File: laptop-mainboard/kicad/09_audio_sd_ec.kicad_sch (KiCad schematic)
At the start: 17 parts, among them U39 ALC256_Codec, U40 GL3224_SD, U41 IT5570E_EC, U42 W25Q128_ECFW

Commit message: Rev B: echte AM5-Pinbelegung, Kleinteile, EliteBook-850-G7-Format
- AM5-Pinmap (1718 Pins, WikiChip/Wikimedia Public Domain) als CSV,
  Sockel-Footprint mit echten Padnamen und 1708 Signal-Netzen im Board
- Blatt 10: MLCC-Baenke, 11 ESD-Arrays, USB2-Chokes, Straps; 48-MHz-Quarz;
  beidseitige Bestueckung (B.Cu) mit Kollisionspruefung pro Seite
- Board 340x112mm im EliteBook-850-G7-Layout: USB-C-100W-PD an der
  Barrel-Jack-Position, TB4/HDMI/USB-A/RJ45 rechts, USB-A/Klinke links,
  HP-Akku 3S/56Wh, HP-FPC-Steckplaetze (Pinouts zu verifizieren)
- GND-Stitching-Vias, MDI-/DP-Korridore, 645 Board-Netze
- Renderer tools/render_board.py erzeugt docs/board_render.png
- Doku: elitebook.md neu, grenzen.md/README/power/layout aktualisiert

Co-Authored-By: Claude Fable 5 <noreply@anthropic.com>
Claude-Session: https://claude.ai/code/session_01E8mU1RUAv938Hs69waADCc
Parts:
- removed J_SD: SD_Slot_PushPush, laptop_mainboard:SD_PUSH, symbol lm:SD_Slot_PushPush_J_SD
- removed U40: GL3224_SD, laptop_mainboard:QFN48_6x6, symbol lm:GL3224_SD_U40
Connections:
- net EN_USBC2 is gone; now on net TB_PWR_EN: U41.40 (TB_PWR_EN)
- net EN_USBC3 is gone; now on net TB_FORCE_PWR: U41.41 (TB_FORCE_PWR)
- net LAN2_PERST# is gone; now on net NVME2_DEVSLP: U41.49 (SSD2_DEVSLP)
- net +3V3_ALW: now also U41.66 (VCC3V3_ALW); no longer U41.69 (VCC3V3_ALW)
- net ECF_CLK: now also U41.63 (ECSPI_CLK); no longer U41.66 (ECSPI_CLK)
- net ECF_CS#: now also U41.62 (ECSPI_CS#); no longer U41.65 (ECSPI_CS#)
- net ECF_MISO: now also U41.65 (ECSPI_MISO); no longer U41.68 (ECSPI_MISO)
- net ECF_MOSI: now also U41.64 (ECSPI_MOSI); no longer U41.67 (ECSPI_MOSI)
- net EDP_BL_EN: now also U41.59 (BL_EN); no longer U41.62 (BL_EN)
- net EDP_BL_PWM: now also U41.60 (BL_PWM); no longer U41.63 (BL_PWM)
- net FAN1_PWM: now also U41.55 (FAN1_PWM); no longer U41.58 (FAN1_PWM)
- net FAN1_TACH: now also U41.56 (FAN1_TACH); no longer U41.59 (FAN1_TACH)
- net FAN2_PWM: now also U41.57 (FAN2_PWM); no longer U41.60 (FAN2_PWM)
- net FAN2_TACH: now also U41.58 (FAN2_TACH); no longer U41.61 (FAN2_TACH)
- net GND: now also U41.67 (GND); no longer U41.70 (GND)
- net KB_BL_CTL: now also U41.61 (KB_BL_CTL); no longer U41.64 (KB_BL_CTL)
- net LAN1_PERST#: now also U41.46 (PE_RST_LAN1#); no longer U41.48 (PE_RST_LAN1#)
- net NVME1_DEVSLP: now also U41.48 (SSD1_DEVSLP); no longer U41.51 (SSD1_DEVSLP)
- net NVME1_PERST#: now also U41.43 (PE_RST_SSD1#); no longer U41.45 (PE_RST_SSD1#)
- net NVME2_DEVSLP: no longer U41.52 (SSD2_DEVSLP)
- net NVME2_PERST#: now also U41.44 (PE_RST_SSD2#); no longer U41.46 (PE_RST_SSD2#)
- net PG_3V3: now also U41.54 (PG_3V3); no longer U41.57 (PG_3V3)
- net PG_5V: now also U41.53 (PG_5V); no longer U41.56 (PG_5V)
- net TB_FORCE_PWR: no longer U41.43 (TB_FORCE_PWR)
- net TB_PERST#: now also U41.45 (PE_RST_TB#); no longer U41.47 (PE_RST_TB#)
- net TB_PWR_EN: no longer U41.42 (TB_PWR_EN)
- net TB_RESET#: now also U41.42 (TB_RESET#); no longer U41.44 (TB_RESET#)
- net VRM_PWRGD: now also U41.52 (VRM_PWRGD); no longer U41.55 (VRM_PWRGD)
- net WIFI_PERST#: now also U41.47 (PE_RST_WIFI#); no longer U41.50 (PE_RST_WIFI#)
- net W_DISABLE1#: now also U41.50 (W_DISABLE1#); no longer U41.53 (W_DISABLE1#)
- net W_DISABLE2#: now also U41.51 (W_DISABLE2#); no longer U41.54 (W_DISABLE2#)
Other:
- note added: "Audio: ALC256 am SoC-HDA-Link; Klinke links wie beim 850 G7."
- note added: "HP-FPC-Pinouts (Tastatur/Touchpad/Akku): docs/elitebook.md."
- note removed: "Audio: ALC256 am SoC-HDA-Link; Klinke = AUX-Kombiport."
- note removed: "SD-Leser GL3224 an USB3-Port 5 des SoC (UHS-II faehig)."
- title: Audio / SD-Leser / Embedded Controller -> Audio / Embedded Controller

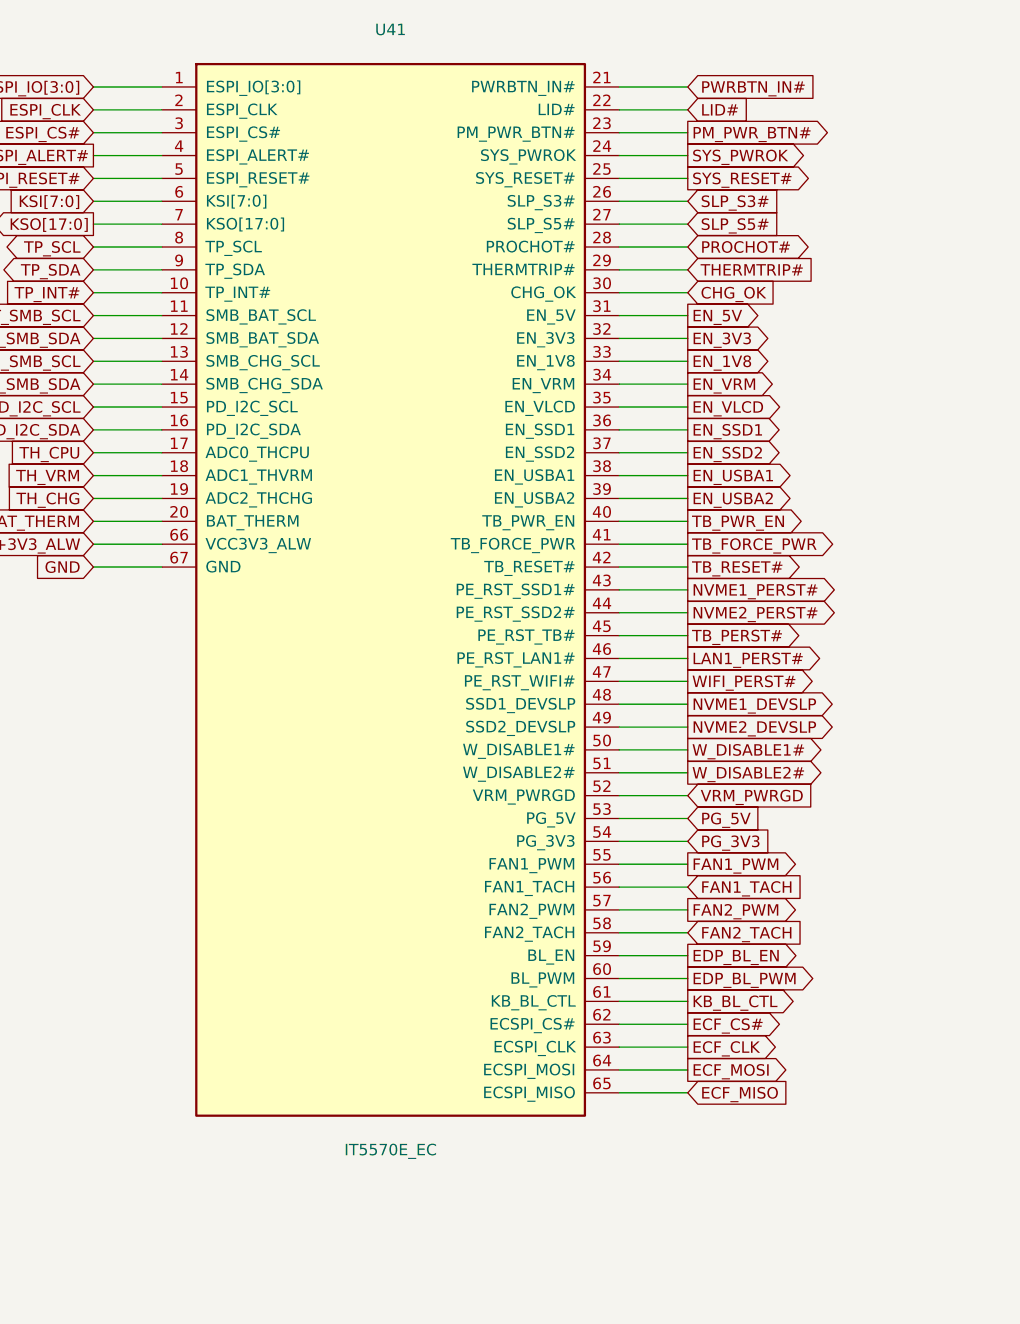
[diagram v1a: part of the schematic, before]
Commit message: Portlayout nach Fotos des Originalgeraets korrigiert
- Rechte Kante hinten->vorn: USB-C-Ladeport 100W (Barrel-Position,
  eigener TPS65987D + Config-Flash, neues Blatt 07_ladeport), USB-A,
  HDMI, 2x USB-C Thunderbolt 4 nebeneinander (JHL8540)
- Kein RJ45 (Original hat keines): Ethernet entfernt, G0/G1 Reserve
- TPS65988 nur noch Source fuer die TB-Ports; breite VBUS_IN-Trasse
  vom Ladeport zum BQ25731
- Interne Anschlusspositionen des Original-Mainboards (Nutzerfoto)
  als Referenztabelle in docs/elitebook.md dokumentiert
- Doku, Blockdiagramm, BOM und Rendering aktualisiert

Co-Authored-By: Claude Fable 5 <noreply@anthropic.com>
Claude-Session: https://claude.ai/code/session_01E8mU1RUAv938Hs69waADCc
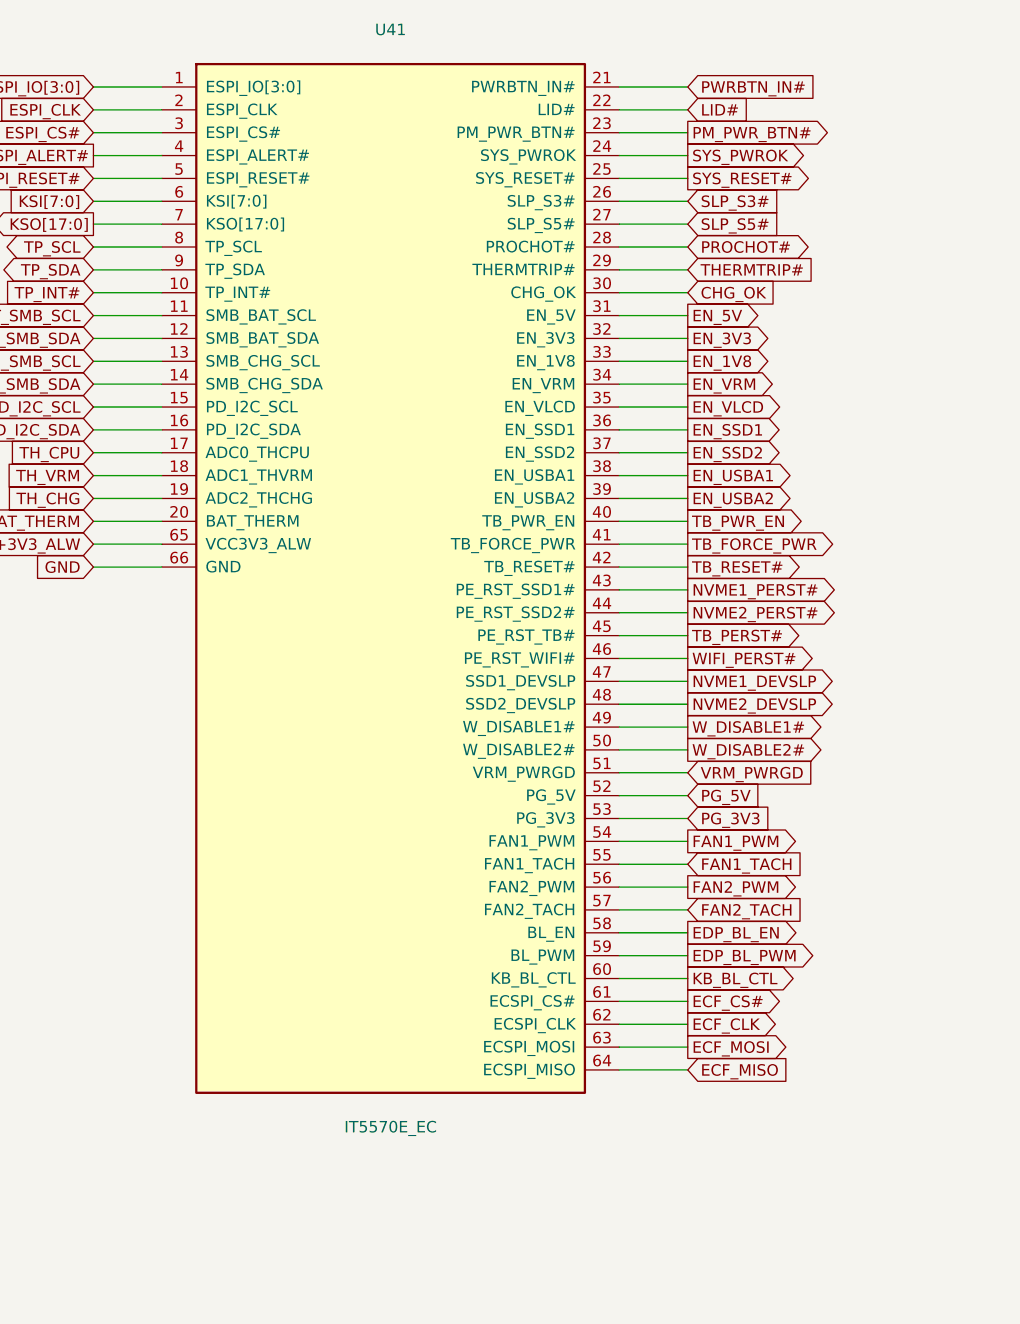
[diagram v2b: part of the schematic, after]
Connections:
- net LAN1_PERST# is gone; now on net WIFI_PERST#: U41.46 (PE_RST_WIFI#)
- net +3V3_ALW: now also U41.65 (VCC3V3_ALW); no longer U41.66 (VCC3V3_ALW)
- net ECF_CLK: now also U41.62 (ECSPI_CLK); no longer U41.63 (ECSPI_CLK)
- net ECF_CS#: now also U41.61 (ECSPI_CS#); no longer U41.62 (ECSPI_CS#)
- net ECF_MISO: now also U41.64 (ECSPI_MISO); no longer U41.65 (ECSPI_MISO)
- net ECF_MOSI: now also U41.63 (ECSPI_MOSI); no longer U41.64 (ECSPI_MOSI)
- net EDP_BL_EN: now also U41.58 (BL_EN); no longer U41.59 (BL_EN)
- net EDP_BL_PWM: now also U41.59 (BL_PWM); no longer U41.60 (BL_PWM)
- net FAN1_PWM: now also U41.54 (FAN1_PWM); no longer U41.55 (FAN1_PWM)
- net FAN1_TACH: now also U41.55 (FAN1_TACH); no longer U41.56 (FAN1_TACH)
- net FAN2_PWM: now also U41.56 (FAN2_PWM); no longer U41.57 (FAN2_PWM)
- net FAN2_TACH: now also U41.57 (FAN2_TACH); no longer U41.58 (FAN2_TACH)
- net GND: now also U41.66 (GND); no longer U41.67 (GND)
- net KB_BL_CTL: now also U41.60 (KB_BL_CTL); no longer U41.61 (KB_BL_CTL)
- net NVME1_DEVSLP: now also U41.47 (SSD1_DEVSLP); no longer U41.48 (SSD1_DEVSLP)
- net NVME2_DEVSLP: now also U41.48 (SSD2_DEVSLP); no longer U41.49 (SSD2_DEVSLP)
- net PG_3V3: now also U41.53 (PG_3V3); no longer U41.54 (PG_3V3)
- net PG_5V: now also U41.52 (PG_5V); no longer U41.53 (PG_5V)
- net VRM_PWRGD: now also U41.51 (VRM_PWRGD); no longer U41.52 (VRM_PWRGD)
- net WIFI_PERST#: no longer U41.47 (PE_RST_WIFI#)
- net W_DISABLE1#: now also U41.49 (W_DISABLE1#); no longer U41.50 (W_DISABLE1#)
- net W_DISABLE2#: now also U41.50 (W_DISABLE2#); no longer U41.51 (W_DISABLE2#)
